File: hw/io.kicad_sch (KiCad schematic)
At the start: 30 parts

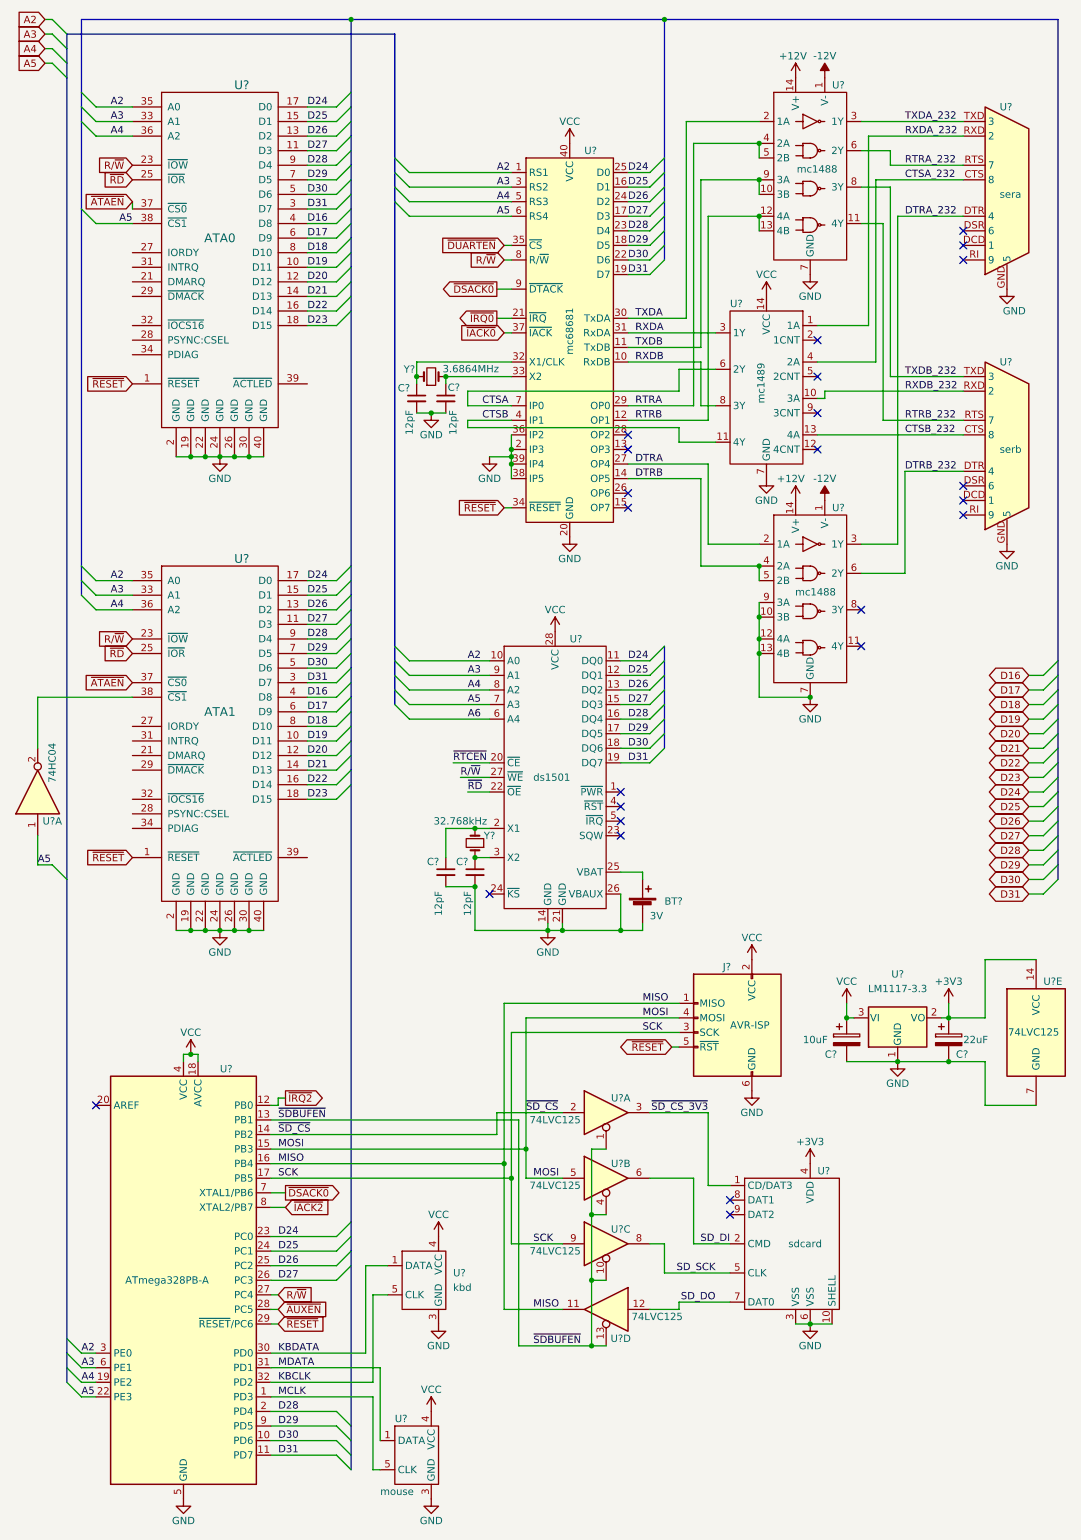
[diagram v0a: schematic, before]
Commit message: expansion, compactflash connector, 3v3reg jumper
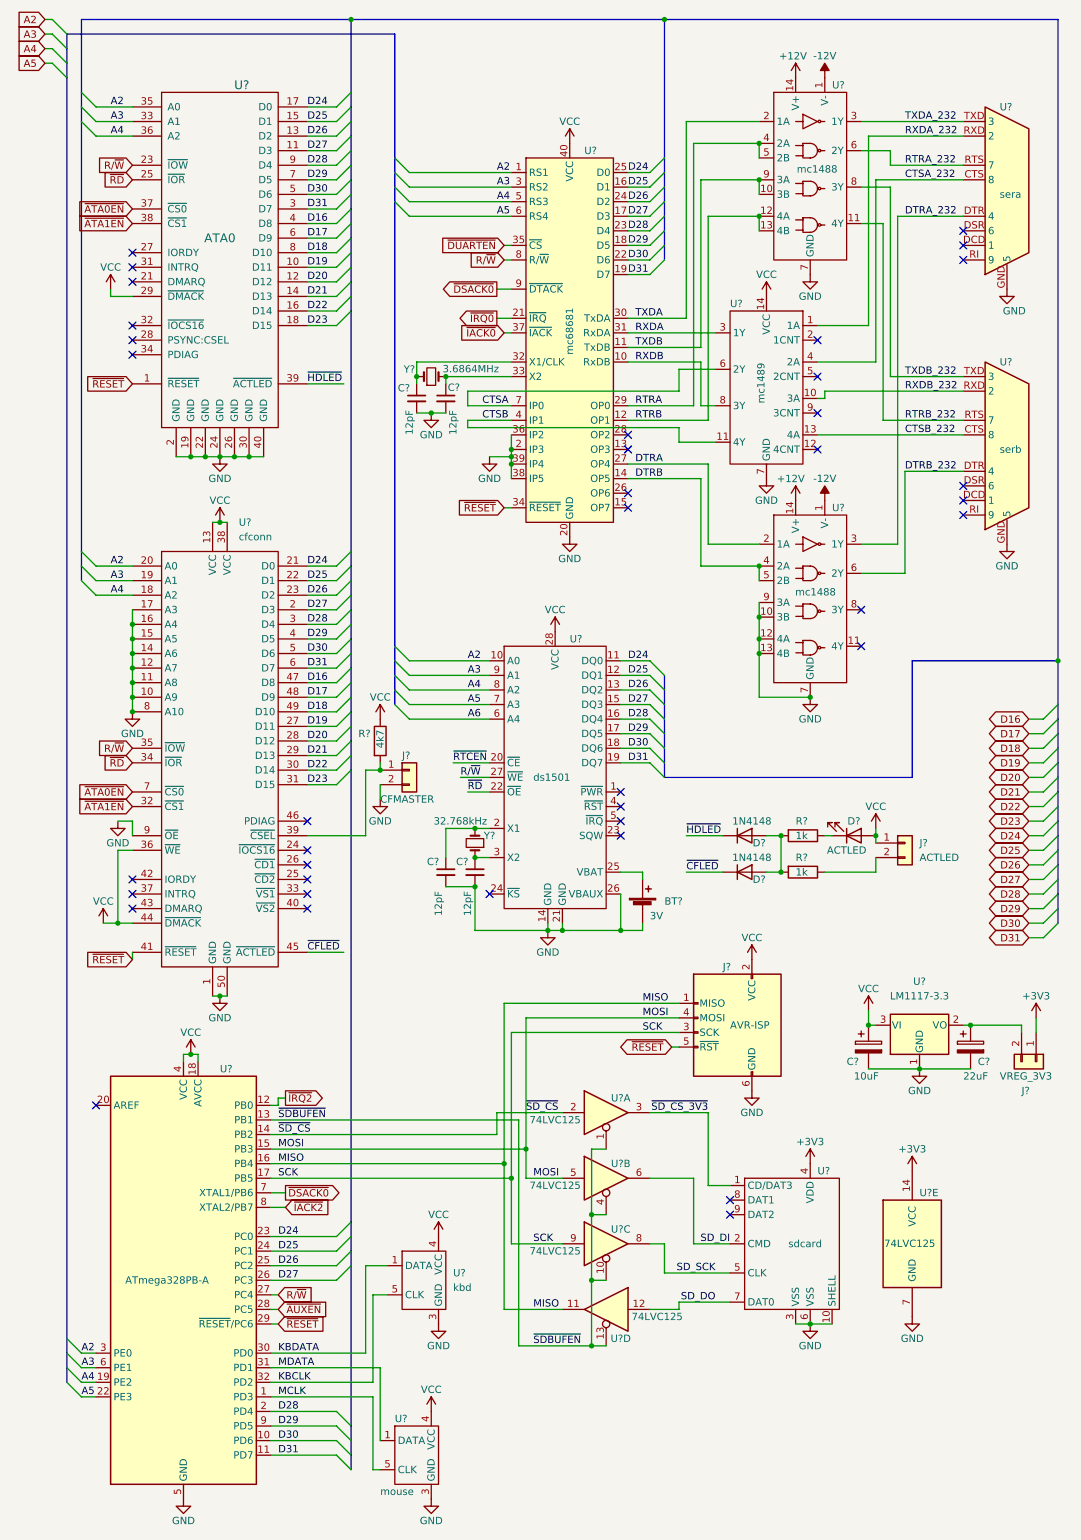
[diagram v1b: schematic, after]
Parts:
- removed U?: ATA1, symbol m68kcomp2:ata_connector
- removed U?: 74HC04, symbol 74xx:74LS04
- added D? (x2): 1N4148, Diode_THT:D_DO-35_SOD27_P7.62mm_Horizontal, symbol Diode:1N4148
- added D?: ACTLED, symbol Device:LED
- added J?: ACTLED, symbol Connector_Generic:Conn_01x02
- added J?: CFMASTER, symbol Connector_Generic:Conn_01x02
- added J?: VREG_3V3, symbol Connector_Generic:Conn_01x02
- added R?: 4k7, OptoDevice:R_LDR_D13.8mm_P9.0mm_Vertical, symbol Device:R
- added R? (x2): 1k, OptoDevice:R_LDR_D13.8mm_P9.0mm_Vertical, symbol Device:R
- added U?: cfconn, symbol m68kcomp2:cfconn
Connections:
- net +3V3: now also J?.1 (Pin_1); no longer C?.1, U?.2 (VO)
- net A2: now also U?.20 (A0)
- net A3: now also U?.19 (A1)
- net A4: now also U?.18 (A2)
- net A5: no longer U?.38 (~{CS1})
- net D16: now also U?.47 (D8)
- net D17: now also U?.48 (D9)
- net D18: now also U?.49 (D10)
- net D19: now also U?.27 (D11)
- net D20: now also U?.28 (D12)
- net D21: now also U?.29 (D13)
- net D22: now also U?.30 (D14)
- net D23: now also U?.31 (D15)
- net D24: now also U?.21 (D0)
- net D25: now also U?.22 (D1)
- net D26: now also U?.23 (D2)
- net D27: now also U?.2 (D3)
- net D28: now also U?.3 (D4)
- net D29: now also U?.4 (D5)
- net D30: now also U?.5 (D6)
- net D31: now also U?.6 (D7)
- net GND: now also J?.2 (Pin_2), U?.1 (GND), U?.10 (A9), U?.11 (A8), U?.12 (A7), U?.14 (A6), U?.15 (A5), U?.16 (A4), U?.17 (A3), U?.50 (GND), U?.8 (A10), U?.9 (~{OE})
- net R/~{W}: now also U?.35 (~{IOW})
- net VCC: now also U?.29 (~{DMACK}), D?.2 (A), J?.1 (Pin_1), R?.1, U?.13 (VCC), U?.36 (~{WE}), U?.38 (VCC), U?.44 (~{DMACK})
- net ~{RD}: now also U?.34 (~{IOR})
- net ~{RESET}: now also U?.41 (~{RESET})
- net ~{HDLED}: now reaches U?.39 (~{ACTLED})
- net ~{HDLED}: now also D?.1 (K)
- net ~{ATAEN} renamed ~{ATA0EN}
- net ~{ATA0EN}: now also U?.7 (~{CS0})
- new net: D?.2 (A), D?.2 (A), R?.2, R?.2
- new net: J?.1 (Pin_1), R?.2, U?.39 (~{CSEL})
- new net: D?.1 (K), R?.1
- new net: J?.2 (Pin_2), R?.1
- new net: C?.1, J?.2 (Pin_2), U?.2 (VO)
- new net ~{ATA1EN}: U?.32 (~{CS1}), U?.38 (~{CS1})
- new net ~{CFLED}: D?.1 (K), U?.45 (~{ACTLED})
- no-connect marks 24 -> 39
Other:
- moved on the sheet: C?, U?, U?E

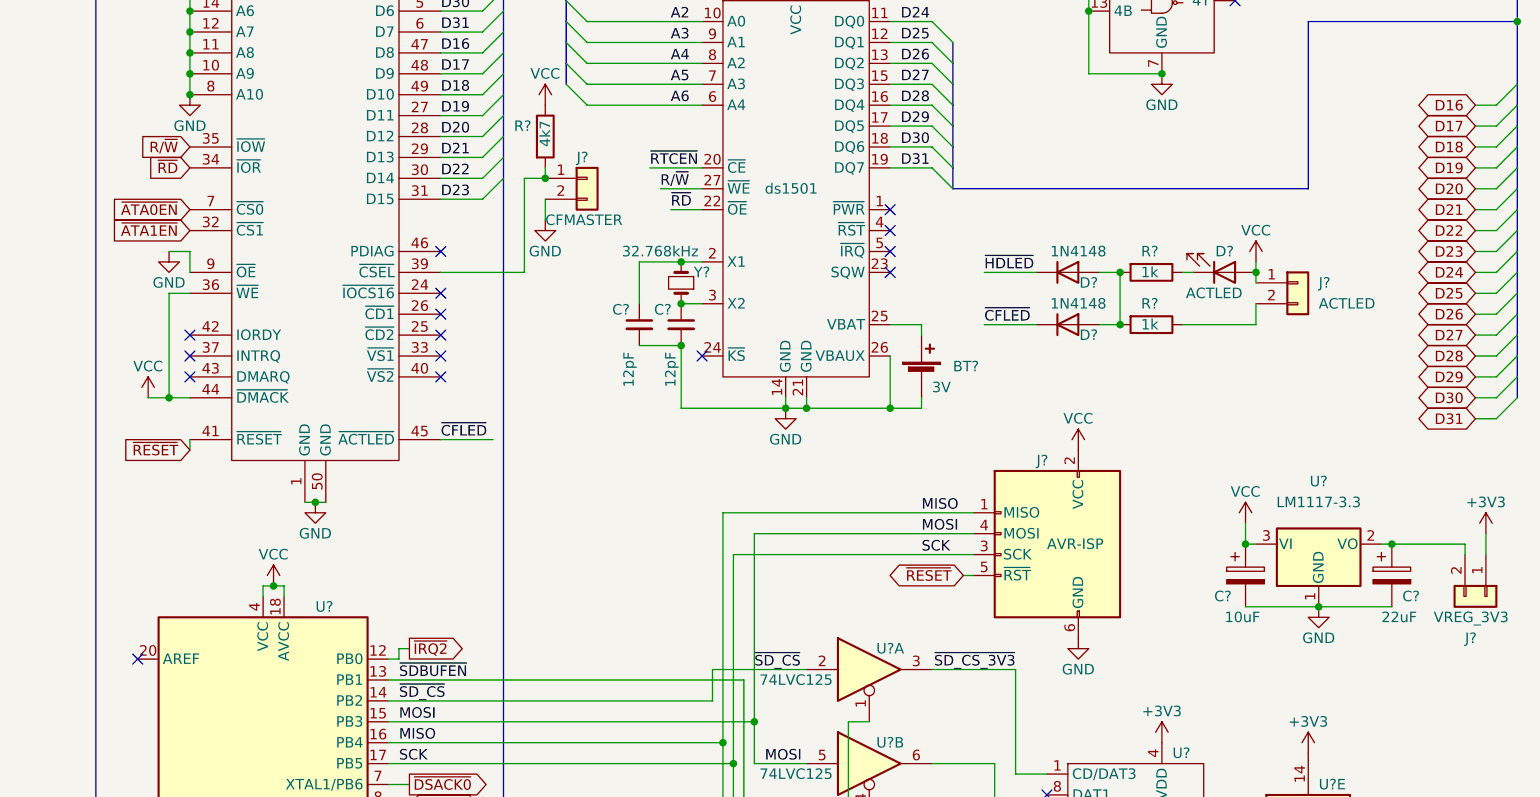
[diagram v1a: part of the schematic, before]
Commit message: separate power sheet
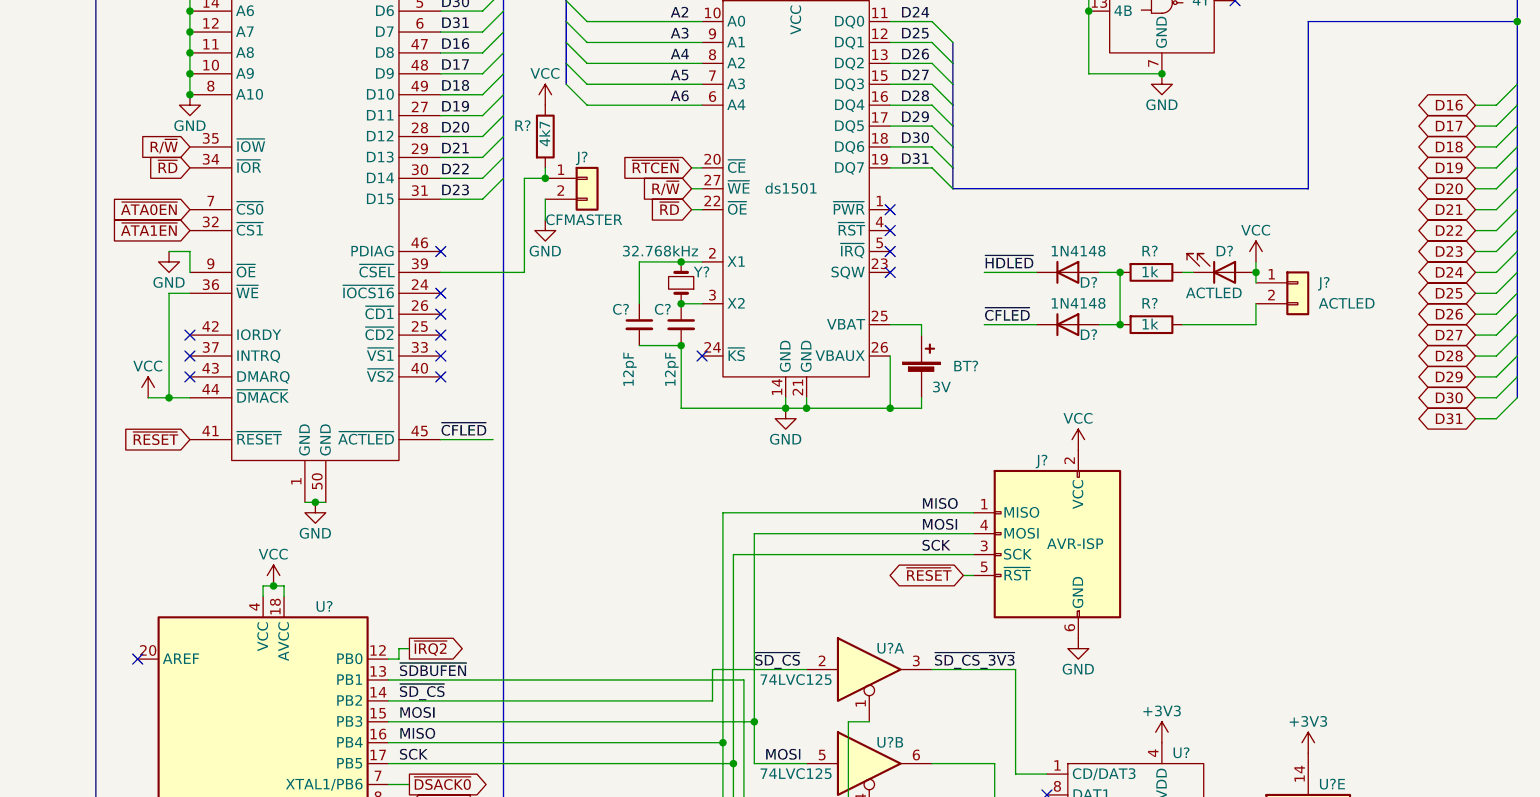
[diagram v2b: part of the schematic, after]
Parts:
- removed C?: 22uF, symbol Device:C_Polarized
- removed C?: 10uF, symbol Device:C_Polarized
- removed J?: VREG_3V3, symbol Connector_Generic:Conn_01x02
- removed U?: LM1117-3.3, symbol Regulator_Linear:LM1117-3.3

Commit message: fixed ERC errors
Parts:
- gave numbers to parts that had none: 30

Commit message: first pass at assigning footprints
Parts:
- BT1: footprint (none) -> Battery:BatteryHolder_Keystone_1060_1x2032
- D9: footprint (none) -> LED_SMD:LED_0805_2012Metric_Pad1.15x1.40mm_HandSolder
- J2, J4: footprint (none) -> Connector_PinHeader_2.54mm:PinHeader_1x02_P2.54mm_Vertical
- J3: footprint (none) -> Connector_IDC:IDC-Header_2x03_P2.54mm_Vertical
- U13: footprint (none) -> Connector_Card:CF-Card_3M_N7E50-7516PK-20-WF
- U14: footprint (none) -> Connector_IDC:IDC-Header_2x20_P2.54mm_Vertical
- U17: footprint (none) -> Package_SO:SOIC-28W_7.5x17.9mm_P1.27mm
- U19: footprint (none) -> Package_SO:SO-14_3.9x8.65mm_P1.27mm
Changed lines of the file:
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@@
       (effects (font (size 1.27 1.27)) (justify left))
     )
-    (property "Footprint" "" (id 2) (at 48.26 143.51 0)
+    (property "Footprint" "Connector_Card:CF-Card_3M_N7E50-7516PK-20-WF" (id 2) (at 48.26 143.51 0)
       (effects (font (size 1.27 1.27)) hide)
     )
@@
     (property "Reference" "D9" (id 0) (at 158.75 158.75 0))
     (property "Value" "ACTLED" (id 1) (at 157.48 163.83 0))
-    (property "Footprint" "" (id 2) (at 158.75 161.29 0)
+    (property "Footprint" "LED_SMD:LED_0805_2012Metric_Pad1.15x1.40mm_HandSolder" (id 2) (at 158.75 161.29 0)
       (effects (font (size 1.27 1.27)) hide)
     )
@@
     (property "Reference" "U19" (id 0) (at 118.11 248.92 0))
     (property "Value" "74LVC125" (id 1) (at 124.46 245.11 0))
-    (property "Footprint" "" (id 2) (at 115.57 243.84 0)
+    (property "Footprint" "Package_SO:SO-14_3.9x8.65mm_P1.27mm" (id 2) (at 115.57 243.84 0)
       (effects (font (size 1.27 1.27)) hide)
     )
@@
       (effects (font (size 1.27 1.27)) (justify left))
     )
-    (property "Footprint" "" (id 2) (at 167.64 162.56 0)
+    (property "Footprint" "Connector_PinHeader_2.54mm:PinHeader_1x02_P2.54mm_Vertical" (id 2) (at 167.64 162.56 0)
       (effects (font (size 1.27 1.27)) hide)
     )
@@
     (property "Reference" "U19" (id 0) (at 118.11 218.44 0))
     (property "Value" "74LVC125" (id 1) (at 106.68 222.25 0))
-    (property "Footprint" "" (id 2) (at 115.57 220.98 0)
+    (property "Footprint" "Package_SO:SO-14_3.9x8.65mm_P1.27mm" (id 2) (at 115.57 220.98 0)
       (effects (font (size 1.27 1.27)) hide)
     )
@@
     (property "Reference" "U19" (id 0) (at 118.11 229.87 0))
     (property "Value" "74LVC125" (id 1) (at 106.68 233.68 0))
-    (property "Footprint" "" (id 2) (at 115.57 232.41 0)
+    (property "Footprint" "Package_SO:SO-14_3.9x8.65mm_P1.27mm" (id 2) (at 115.57 232.41 0)
       (effects (font (size 1.27 1.27)) hide)
     )
@@
       (effects (font (size 1.27 1.27)) (justify left))
     )
-    (property "Footprint" "" (id 2) (at 168.91 232.41 0)
+    (property "Footprint" "Package_SO:SO-14_3.9x8.65mm_P1.27mm" (id 2) (at 168.91 232.41 0)
       (effects (font (size 1.27 1.27)) hide)
     )
@@
       (effects (font (size 1.524 1.524)))
     )
-    (property "Footprint" "" (id 2) (at 35.56 74.93 0)
+    (property "Footprint" "Connector_IDC:IDC-Header_2x20_P2.54mm_Vertical" (id 2) (at 35.56 74.93 0)
       (effects (font (size 1.524 1.524)) hide)
     )
@@
       (effects (font (size 1.27 1.27)) (justify left))
     )
-    (property "Footprint" "" (id 2) (at 106.68 166.37 0)
+    (property "Footprint" "Package_SO:SOIC-28W_7.5x17.9mm_P1.27mm" (id 2) (at 106.68 166.37 0)
       (effects (font (size 1.27 1.27)) hide)
     )
@@
       (effects (font (size 1.27 1.27)) (justify left))
     )
-    (property "Footprint" "" (id 2) (at 81.28 149.86 0)
+    (property "Footprint" "Connector_PinHeader_2.54mm:PinHeader_1x02_P2.54mm_Vertical" (id 2) (at 81.28 149.86 0)
       (effects (font (size 1.27 1.27)) hide)
     )
@@
       (effects (font (size 1.27 1.27)) (justify left))
     )
-    (property "Footprint" "" (id 2) (at 121.92 172.466 90)
+    (property "Footprint" "Battery:BatteryHolder_Keystone_1060_1x2032" (id 2) (at 121.92 172.466 90)
       (effects (font (size 1.27 1.27)) hide)
     )
@@
     (property "Reference" "U19" (id 0) (at 118.11 207.01 0))
     (property "Value" "74LVC125" (id 1) (at 106.68 210.82 0))
-    (property "Footprint" "" (id 2) (at 115.57 209.55 0)
+    (property "Footprint" "Package_SO:SO-14_3.9x8.65mm_P1.27mm" (id 2) (at 115.57 209.55 0)
       (effects (font (size 1.27 1.27)) hide)
     )
@@
       (effects (font (size 1.27 1.27)) (justify right))
     )
-    (property "Footprint" "" (id 2) (at 144.78 194.31 90)
-      (effects (font (size 1.27 1.27)) hide)
-    )
+    (property "Footprint" "Connector_IDC:IDC-Header_2x03_P2.54mm_Vertical" (id 2) (at 144.78 194.31 90)
+      (effects (font (size 1.27 1.27)) hide)
+    )

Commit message: finished the footprints
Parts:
- U15, U16: footprint (none) -> m68kcomp2:minidin6
- U23: footprint (none) -> Connector_Card:SD_TE_2041021
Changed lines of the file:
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@@
       (effects (font (size 1.27 1.27)) (justify left))
     )
-    (property "Footprint" "" (id 2) (at 151.13 232.41 0)
+    (property "Footprint" "Connector_Card:SD_TE_2041021" (id 2) (at 151.13 232.41 0)
       (effects (font (size 1.27 1.27)) hide)
     )
@@
       (effects (font (size 1.27 1.27)) (justify left))
     )
-    (property "Footprint" "" (id 2) (at 83.82 269.24 0)
+    (property "Footprint" "m68kcomp2:minidin6" (id 2) (at 83.82 269.24 0)
       (effects (font (size 1.27 1.27)) hide)
     )
@@
       (effects (font (size 1.27 1.27)) (justify left))
     )
-    (property "Footprint" "" (id 2) (at 85.09 238.76 0)
-      (effects (font (size 1.27 1.27)) hide)
-    )
+    (property "Footprint" "m68kcomp2:minidin6" (id 2) (at 85.09 238.76 0)
+      (effects (font (size 1.27 1.27)) hide)
+    )
